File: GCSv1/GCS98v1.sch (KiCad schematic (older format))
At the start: 23 parts, among them U1 STM32F303CCTx

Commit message: fixed switches in matrix, ready for layout
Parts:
- removed U?: LD3985M33R_SOT23, Package_TO_SOT_SMD:SOT-23-5, symbol Regulator_Linear:LD3985M33R_SOT23
- added U2: LD3985M33R_SOT23, Package_TO_SOT_SMD:SOT-23-5, symbol Regulator_Linear:LD3985M33R_SOT23
- C10, C11, C12, C13, C14, C15, C16, C17, C7, C8, C9: renamed from C?; footprint (none) -> Capacitor_SMD:C_0805_2012Metric_Pad1.18x1.45mm_HandSolder
- C18: renamed from 100nF; value C -> 100nF; footprint (none) -> Capacitor_SMD:C_0805_2012Metric_Pad1.18x1.45mm_HandSolder
- R2, R3, R4, R5: renamed from R?; footprint (none) -> Resistor_SMD:R_0805_2012Metric_Pad1.20x1.40mm_HandSolder
- SW99: renamed from SW?; footprint (none) -> Button_Switch_SMD:SW_SPST_SKQG_WithStem
- Y1: renamed from Y?; footprint (none) -> Crystal:Crystal_SMD_3225-4Pin_3.2x2.5mm_HandSoldering
- gave numbers to parts that had none: 3
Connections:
- net +5V: now also U2.1 (VIN), U2.3 (INH)
- net GND: now also U2.2 (GND)
- net at C10.1: now also U2.4 (BYP)
- net at C11.1, C8.1, D197.2 (A): now also U2.5 (VOUT)
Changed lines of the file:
@@
 $EndSheet
 $Comp
-L Connector_Generic:Conn_01x04 J?
+L Connector_Generic:Conn_01x04 J1
 U 1 1 6100B131
 P 5900 4550
-F 0 "J?" H 5980 4542 50  0000 L CNN
+F 0 "J1" H 5980 4542 50  0000 L CNN
 F 1 "SM04B-SRSS-TB(LF)(SN)" H 5980 4451 50  0000 L CNN
 F 2 "random-keyboard-parts:JST-SR-4" H 5900 4550 50  0001 C CNN
@@
 	3750 2150 3650 2150
 $Comp
-L Regulator_Linear:LD3985M33R_SOT23 U?
-U 1 1 61021750
-P 3800 1100
-F 0 "U?" H 3800 1442 50  0000 C CNN
-F 1 "LD3985M33R_SOT23" H 3800 1351 50  0000 C CNN
-F 2 "Package_TO_SOT_SMD:SOT-23-5" H 3800 1425 50  0001 C CIN
-F 3 "http://www.st.com/internet/com/TECHNICAL_RESOURCES/TECHNICAL_LITERATURE/DATASHEET/CD00003395.pdf" H 3800 1100 50  0001 C CNN
-	1    3800 1100
-	1    0    0    -1
-$EndComp
-$Comp
 L power:+3V3 #PWR0103
 U 1 1 6102369C
@@
 $EndComp
 $Comp
-L Device:C C?
+L Device:C C7
 U 1 1 610250E6
 P 3100 1250
-F 0 "C?" H 3215 1296 50  0000 L CNN
+F 0 "C7" H 3215 1296 50  0000 L CNN
 F 1 "1µF" H 3215 1205 50  0000 L CNN
-F 2 "" H 3138 1100 50  0001 C CNN
+F 2 "Capacitor_SMD:C_0805_2012Metric_Pad1.18x1.45mm_HandSolder" H 3138 1100 50  0001 C CNN
 F 3 "~" H 3100 1250 50  0001 C CNN
 	1    3100 1250
@@
 	3100 1000 3100 1100
 $Comp
-L Device:C C?
+L Device:C C9
 U 1 1 6102C881
 P 3400 1400
-F 0 "C?" H 3515 1446 50  0000 L CNN
+F 0 "C9" H 3515 1446 50  0000 L CNN
 F 1 "100nF" H 3515 1355 50  0000 L CNN
-F 2 "" H 3438 1250 50  0001 C CNN
+F 2 "Capacitor_SMD:C_0805_2012Metric_Pad1.18x1.45mm_HandSolder" H 3438 1250 50  0001 C CNN
 F 3 "~" H 3400 1400 50  0001 C CNN
 	1    3400 1400
@@
 $EndComp
 $Comp
-L Device:C C?
+L Device:C C10
 U 1 1 6102FE4B
 P 4150 1400
-F 0 "C?" H 4265 1446 50  0000 L CNN
+F 0 "C10" H 4265 1446 50  0000 L CNN
 F 1 "10nF" H 4265 1355 50  0000 L CNN
-F 2 "" H 4188 1250 50  0001 C CNN
+F 2 "Capacitor_SMD:C_0805_2012Metric_Pad1.18x1.45mm_HandSolder" H 4188 1250 50  0001 C CNN
 F 3 "~" H 4150 1400 50  0001 C CNN
 	1    4150 1400
@@
 $EndComp
 $Comp
-L Device:C C?
+L Device:C C8
 U 1 1 61037105
 P 4500 1250
-F 0 "C?" H 4615 1296 50  0000 L CNN
+F 0 "C8" H 4615 1296 50  0000 L CNN
 F 1 "100nF" H 4615 1205 50  0000 L CNN
-F 2 "" H 4538 1100 50  0001 C CNN
+F 2 "Capacitor_SMD:C_0805_2012Metric_Pad1.18x1.45mm_HandSolder" H 4538 1100 50  0001 C CNN
 F 3 "~" H 4500 1250 50  0001 C CNN
 	1    4500 1250
@@
 	4500 1100 4500 1000
 $Comp
-L Device:C C?
+L Device:C C11
 U 1 1 61039CE0
 P 4900 1400
-F 0 "C?" H 5015 1446 50  0000 L CNN
+F 0 "C11" H 5015 1446 50  0000 L CNN
 F 1 "100nF" H 5015 1355 50  0000 L CNN
-F 2 "" H 4938 1250 50  0001 C CNN
+F 2 "Capacitor_SMD:C_0805_2012Metric_Pad1.18x1.45mm_HandSolder" H 4938 1250 50  0001 C CNN
 F 3 "~" H 4900 1400 50  0001 C CNN
 	1    4900 1400
@@
 $EndComp
 $Comp
-L Diode:BAT60A D?
+L Diode:BAT60A D197
 U 1 1 6103C710
 P 5150 1000
-F 0 "D?" H 5150 783 50  0000 C CNN
+F 0 "D197" H 5150 783 50  0000 C CNN
 F 1 "BAT60A" H 5150 874 50  0000 C CNN
 F 2 "Diode_SMD:D_SOD-323" H 5150 825 50  0001 C CNN
@@
 $EndComp
 $Comp
-L Device:C C?
+L Device:C C12
 U 1 1 6109CA20
 P 5000 2900
-F 0 "C?" H 5115 2946 50  0000 L CNN
+F 0 "C12" H 5115 2946 50  0000 L CNN
 F 1 "100nF" H 5115 2855 50  0000 L CNN
-F 2 "" H 5038 2750 50  0001 C CNN
+F 2 "Capacitor_SMD:C_0805_2012Metric_Pad1.18x1.45mm_HandSolder" H 5038 2750 50  0001 C CNN
 F 3 "~" H 5000 2900 50  0001 C CNN
 	1    5000 2900
@@
 $EndComp
 $Comp
-L Device:C C?
+L Device:C C13
 U 1 1 6109D7C4
 P 5450 2900
-F 0 "C?" H 5565 2946 50  0000 L CNN
+F 0 "C13" H 5565 2946 50  0000 L CNN
 F 1 "100nF" H 5565 2855 50  0000 L CNN
-F 2 "" H 5488 2750 50  0001 C CNN
+F 2 "Capacitor_SMD:C_0805_2012Metric_Pad1.18x1.45mm_HandSolder" H 5488 2750 50  0001 C CNN
 F 3 "~" H 5450 2900 50  0001 C CNN
 	1    5450 2900
@@
 $EndComp
 $Comp
-L Device:C C?
+L Device:C C14
 U 1 1 610A0182
 P 5900 2900
-F 0 "C?" H 6015 2946 50  0000 L CNN
+F 0 "C14" H 6015 2946 50  0000 L CNN
 F 1 "100nF" H 6015 2855 50  0000 L CNN
-F 2 "" H 5938 2750 50  0001 C CNN
+F 2 "Capacitor_SMD:C_0805_2012Metric_Pad1.18x1.45mm_HandSolder" H 5938 2750 50  0001 C CNN
 F 3 "~" H 5900 2900 50  0001 C CNN
 	1    5900 2900
@@
 $EndComp
 $Comp
-L Device:C C?
+L Device:C C15
 U 1 1 610A0188
 P 6350 2900
-F 0 "C?" H 6465 2946 50  0000 L CNN
+F 0 "C15" H 6465 2946 50  0000 L CNN
 F 1 "100nF" H 6465 2855 50  0000 L CNN
-F 2 "" H 6388 2750 50  0001 C CNN
+F 2 "Capacitor_SMD:C_0805_2012Metric_Pad1.18x1.45mm_HandSolder" H 6388 2750 50  0001 C CNN
 F 3 "~" H 6350 2900 50  0001 C CNN
 	1    6350 2900
@@
 Connection ~ 3750 2150
 $Comp
-L Device:C 100nF
+L Device:C C18
 U 1 1 610C060F
 P 1100 2650
-F 0 "100nF" V 848 2650 50  0000 C CNN
-F 1 "C" V 939 2650 50  0000 C CNN
-F 2 "" H 1138 2500 50  0001 C CNN
+F 0 "C18" V 848 2650 50  0000 C CNN
+F 1 "100nF" V 939 2650 50  0000 C CNN
+F 2 "Capacitor_SMD:C_0805_2012Metric_Pad1.18x1.45mm_HandSolder" H 1138 2500 50  0001 C CNN
 F 3 "~" H 1100 2650 50  0001 C CNN
 	1    1100 2650
@@
 $EndComp
 $Comp
-L Switch:SW_Push SW?
+L Switch:SW_Push SW99
 U 1 1 610C66B5
 P 1100 2300
-F 0 "SW?" H 1100 2585 50  0000 C CNN
+F 0 "SW99" H 1100 2585 50  0000 C CNN
 F 1 "SW_Push" H 1100 2494 50  0000 C CNN
-F 2 "" H 1100 2500 50  0001 C CNN
+F 2 "Button_Switch_SMD:SW_SPST_SKQG_WithStem" H 1100 2500 50  0001 C CNN
 F 3 "~" H 1100 2500 50  0001 C CNN
 	1    1100 2300
@@
 Connection ~ 3550 5250
 $Comp
-L Device:R R?
+L Device:R R3
 U 1 1 610E8EAE
 P 800 3200
-F 0 "R?" H 870 3246 50  0000 L CNN
+F 0 "R3" H 870 3246 50  0000 L CNN
 F 1 "100K" H 870 3155 50  0000 L CNN
-F 2 "" V 730 3200 50  0001 C CNN
+F 2 "Resistor_SMD:R_0805_2012Metric_Pad1.20x1.40mm_HandSolder" V 730 3200 50  0001 C CNN
 F 3 "~" H 800 3200 50  0001 C CNN
 	1    800  3200
@@
 	800  3350 800  3450
 $Comp
-L Diode:BAT60A D?
+L Diode:BAT60A D198
 U 1 1 610F621C
 P 5600 4100
-F 0 "D?" H 5600 3883 50  0000 C CNN
+F 0 "D198" H 5600 3883 50  0000 C CNN
 F 1 "BAT60A" H 5600 3974 50  0000 C CNN
 F 2 "Diode_SMD:D_SOD-323" H 5600 3925 50  0001 C CNN
@@
 Connection ~ 3550 2150
 $Comp
-L Device:Crystal_GND24 Y?
+L Device:Crystal_GND24 Y1
 U 1 1 61135795
 P 1500 4050
-F 0 "Y?" H 1694 4096 50  0000 L CNN
+F 0 "Y1" H 1694 4096 50  0000 L CNN
 F 1 "16MHz" H 1694 4005 50  0000 L CNN
-F 2 "" H 1500 4050 50  0001 C CNN
+F 2 "Crystal:Crystal_SMD_3225-4Pin_3.2x2.5mm_HandSoldering" H 1500 4050 50  0001 C CNN
 F 3 "~" H 1500 4050 50  0001 C CNN
 	1    1500 4050
@@
 $EndComp
 $Comp
-L Device:C C?
+L Device:C C16
 U 1 1 611423E1
 P 1100 4350
-F 0 "C?" H 1215 4396 50  0000 L CNN
+F 0 "C16" H 1215 4396 50  0000 L CNN
 F 1 "20pF" H 1215 4305 50  0000 L CNN
-F 2 "" H 1138 4200 50  0001 C CNN
+F 2 "Capacitor_SMD:C_0805_2012Metric_Pad1.18x1.45mm_HandSolder" H 1138 4200 50  0001 C CNN
 F 3 "~" H 1100 4350 50  0001 C CNN
 	1    1100 4350
@@
 $EndComp
 $Comp
-L Device:C C?
+L Device:C C17
 U 1 1 61143C72
 P 2000 4350
-F 0 "C?" H 2115 4396 50  0000 L CNN
+F 0 "C17" H 2115 4396 50  0000 L CNN
 F 1 "20pF" H 2115 4305 50  0000 L CNN
-F 2 "" H 2038 4200 50  0001 C CNN
+F 2 "Capacitor_SMD:C_0805_2012Metric_Pad1.18x1.45mm_HandSolder" H 2038 4200 50  0001 C CNN
 F 3 "~" H 2000 4350 50  0001 C CNN
 	1    2000 4350
@@
 $EndComp
 $Comp
-L Device:R R?
+L Device:R R2
 U 1 1 611663E7
 P 2300 3000
-F 0 "R?" V 2093 3000 50  0000 C CNN
+F 0 "R2" V 2093 3000 50  0000 C CNN
 F 1 "10K" V 2184 3000 50  0000 C CNN
-F 2 "" V 2230 3000 50  0001 C CNN
+F 2 "Resistor_SMD:R_0805_2012Metric_Pad1.20x1.40mm_HandSolder" V 2230 3000 50  0001 C CNN
 F 3 "~" H 2300 3000 50  0001 C CNN
 	1    2300 3000
@@
 $EndComp
 $Comp
-L Device:R R?
+L Device:R R4
 U 1 1 6117749F
 P 2300 3300
-F 0 "R?" V 2093 3300 50  0000 C CNN
+F 0 "R4" V 2093 3300 50  0000 C CNN
 F 1 "10K" V 2184 3300 50  0000 C CNN
-F 2 "" V 2230 3300 50  0001 C CNN
+F 2 "Resistor_SMD:R_0805_2012Metric_Pad1.20x1.40mm_HandSolder" V 2230 3300 50  0001 C CNN
 F 3 "~" H 2300 3300 50  0001 C CNN
 	1    2300 3300
@@
 $EndComp
 $Comp
-L Device:R R?
+L Device:R R5
 U 1 1 61080E46
 P 5200 4450
-F 0 "R?" H 5270 4496 50  0000 L CNN
+F 0 "R5" H 5270 4496 50  0000 L CNN
 F 1 "1K5" H 5270 4405 50  0000 L CNN
-F 2 "" V 5130 4450 50  0001 C CNN
+F 2 "Resistor_SMD:R_0805_2012Metric_Pad1.20x1.40mm_HandSolder" V 5130 4450 50  0001 C CNN
 F 3 "~" H 5200 4450 50  0001 C CNN
 	1    5200 4450
 	1    0    0    -1
 $EndComp
+$Comp
+L Regulator_Linear:LD3985M33R_SOT23 U2
+U 1 1 66DF6094
+P 3800 1100
+F 0 "U2" H 3800 1442 50  0000 C CNN
+F 1 "LD3985M33R_SOT23" H 3800 1351 50  0000 C CNN
+F 2 "Package_TO_SOT_SMD:SOT-23-5" H 3800 1425 50  0001 C CIN
+F 3 "http://www.st.com/internet/com/TECHNICAL_RESOURCES/TECHNICAL_LITERATURE/DATASHEET/CD00003395.pdf" H 3800 1100 50  0001 C CNN
+	1    3800 1100
+	1    0    0    -1
+$EndComp

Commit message: preliminary work on USB hub
The Texas Instruments USB hub that is currently in there seems like the ticket, but I am still not sure about how USB C connectors will work with the hub IC since it is only for USB 2.0. The main issue is that USB 3.0 and up natively support 3 different power delivery modes up to 15W (and USB power delivery supporting up to 100W), but this is higher than USB 2.0 capabilities and I don't want to fry the thing.
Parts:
- removed D198: BAT60A, Diode_SMD:D_SOD-323, symbol Diode:BAT60A
- removed J1: SM04B-SRSS-TB(LF)(SN), random-keyboard-parts:JST-SR-4, symbol Connector_Generic:Conn_01x04
- removed R5: 1K5, Resistor_SMD:R_0805_2012Metric_Pad1.20x1.40mm_HandSolder, symbol Device:R
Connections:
- net DN renamed DN1
- net DP renamed DP1
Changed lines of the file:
@@
 $Descr A4 11693 8268
 encoding utf-8
-Sheet 1 2
+Sheet 1 3
 Title ""
 Date ""
@@
 F1 "matrix.sch" 50
 $EndSheet
-$Comp
-L Connector_Generic:Conn_01x04 J1
-U 1 1 6100B131
-P 5900 4550
-F 0 "J1" H 5980 4542 50  0000 L CNN
-F 1 "SM04B-SRSS-TB(LF)(SN)" H 5980 4451 50  0000 L CNN
-F 2 "random-keyboard-parts:JST-SR-4" H 5900 4550 50  0001 C CNN
-F 3 "~" H 5900 4550 50  0001 C CNN
-	1    5900 4550
-	1    0    0    -1
-$EndComp
-$Comp
-L power:+5V #PWR0101
-U 1 1 6100BF06
-P 5600 3950
-F 0 "#PWR0101" H 5600 3800 50  0001 C CNN
-F 1 "+5V" H 5615 4123 50  0000 C CNN
-F 2 "" H 5600 3950 50  0001 C CNN
-F 3 "" H 5600 3950 50  0001 C CNN
-	1    5600 3950
-	1    0    0    -1
-$EndComp
-$Comp
-L power:GND #PWR0102
-U 1 1 6100D0BD
-P 5600 4850
-F 0 "#PWR0102" H 5600 4600 50  0001 C CNN
-F 1 "GND" H 5605 4677 50  0000 C CNN
-F 2 "" H 5600 4850 50  0001 C CNN
-F 3 "" H 5600 4850 50  0001 C CNN
-	1    5600 4850
-	1    0    0    -1
-$EndComp
-Wire Wire Line
-	5700 4750 5600 4750
-Wire Wire Line
-	5600 4750 5600 4850
-Wire Wire Line
-	5700 4450 5600 4450
-Wire Wire Line
-	5700 4550 5600 4550
-Text GLabel 5600 4550 0    50   Input ~ 0
-DN
 Text GLabel 4250 4700 2    50   Input ~ 0
-DP
+DP1
 Text GLabel 4250 4600 2    50   Input ~ 0
-DN
+DN1
 $Comp
 L MCU_ST_STM32F3:STM32F303CCTx U1
@@
 Wire Wire Line
 	800  3350 800  3450
-$Comp
-L Diode:BAT60A D198
-U 1 1 610F621C
-P 5600 4100
-F 0 "D198" H 5600 3883 50  0000 C CNN
-F 1 "BAT60A" H 5600 3974 50  0000 C CNN
-F 2 "Diode_SMD:D_SOD-323" H 5600 3925 50  0001 C CNN
-F 3 "https://www.digikey.com/en/products/detail/stmicroelectronics/BAT60JFILM/686386" H 5600 4100 50  0001 C CNN
-	1    5600 4100
-	0    1    1    0
-$EndComp
-Wire Wire Line
-	5600 4250 5600 4450
 Text GLabel 1400 2650 2    50   Input ~ 0
 NRST
@@
 Wire Wire Line
 	2600 3200 2950 3200
-Text GLabel 5100 4650 0    50   Input ~ 0
-DP
-Wire Wire Line
-	5200 4650 5100 4650
-Wire Wire Line
-	5200 4650 5700 4650
-Connection ~ 5200 4650
-Wire Wire Line
-	5200 4600 5200 4650
-Wire Wire Line
-	5200 4300 5200 4200
-$Comp
-L power:+3V3 #PWR0116
-U 1 1 61081D73
-P 5200 4200
-F 0 "#PWR0116" H 5200 4050 50  0001 C CNN
-F 1 "+3V3" H 5215 4373 50  0000 C CNN
-F 2 "" H 5200 4200 50  0001 C CNN
-F 3 "" H 5200 4200 50  0001 C CNN
-	1    5200 4200
-	1    0    0    -1
-$EndComp
-$Comp
-L Device:R R5
-U 1 1 61080E46
-P 5200 4450
-F 0 "R5" H 5270 4496 50  0000 L CNN
-F 1 "1K5" H 5270 4405 50  0000 L CNN
-F 2 "Resistor_SMD:R_0805_2012Metric_Pad1.20x1.40mm_HandSolder" V 5130 4450 50  0001 C CNN
-F 3 "~" H 5200 4450 50  0001 C CNN
-	1    5200 4450
-	1    0    0    -1
-$EndComp
 $Comp
 L Regulator_Linear:LD3985M33R_SOT23 U2
@@
 	1    0    0    -1
 $EndComp
+$Sheet
+S 7550 900  3050 850
+U 611E8410
+F0 "USB_hub" 50
+F1 "USB_hub.sch" 50
+$EndSheet
 $EndSCHEMATC

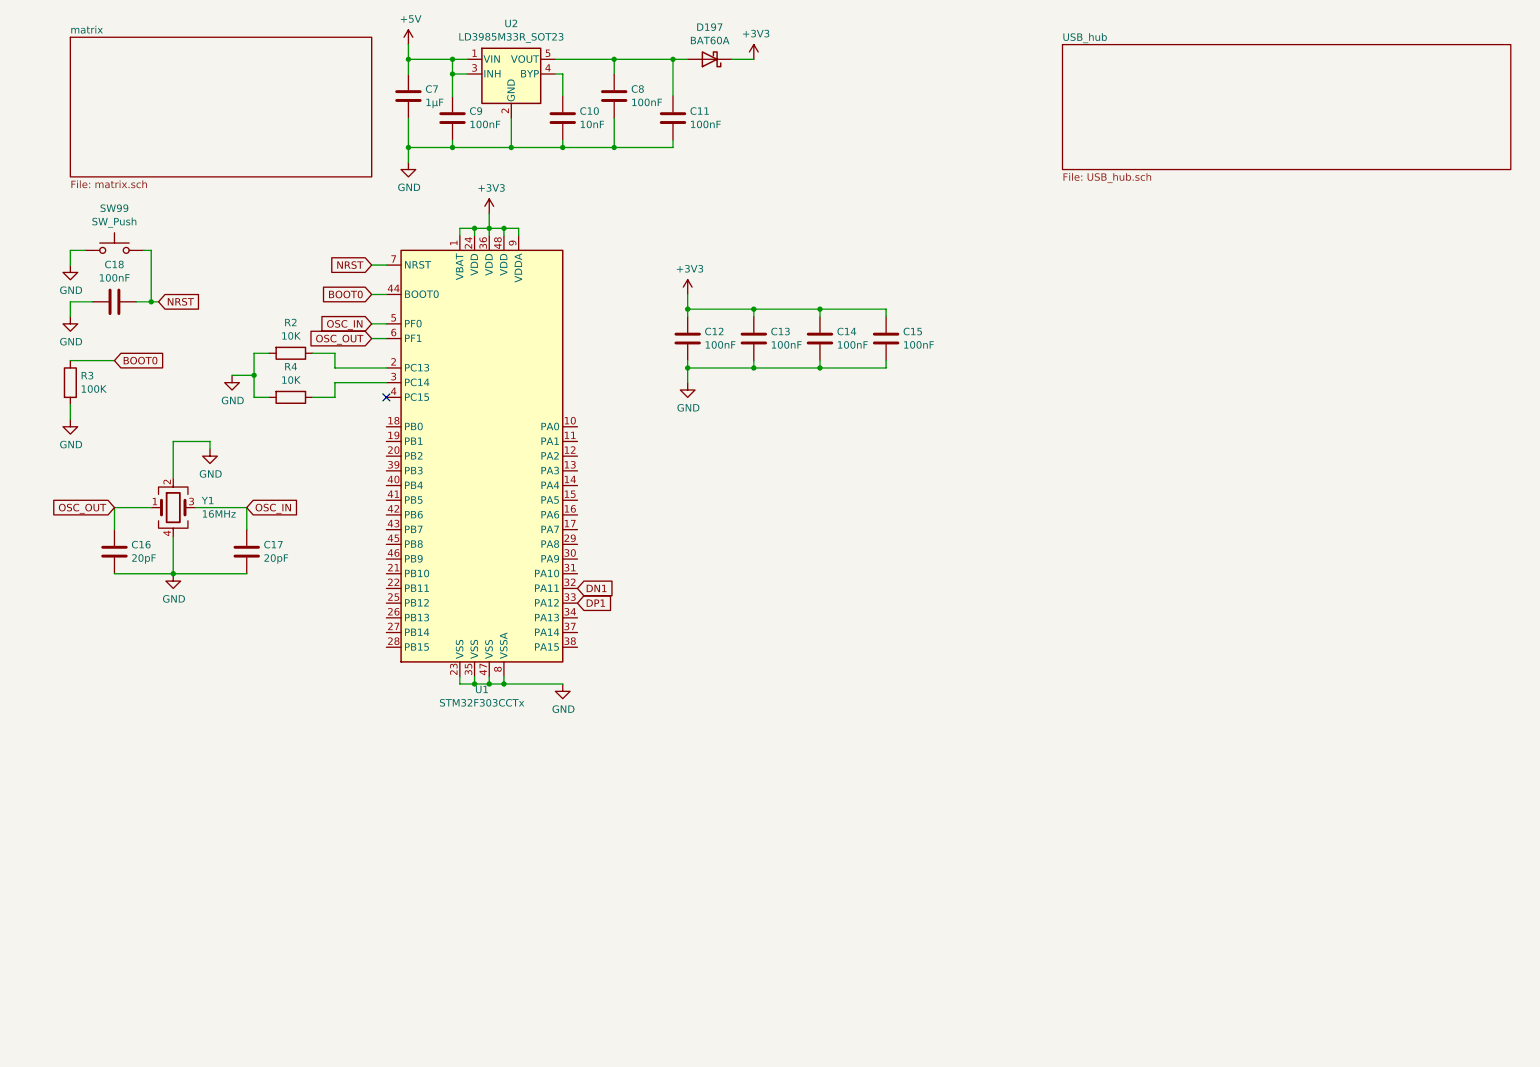
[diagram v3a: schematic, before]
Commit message: redid matrix routing, not doing USB daughter board because of parts availability
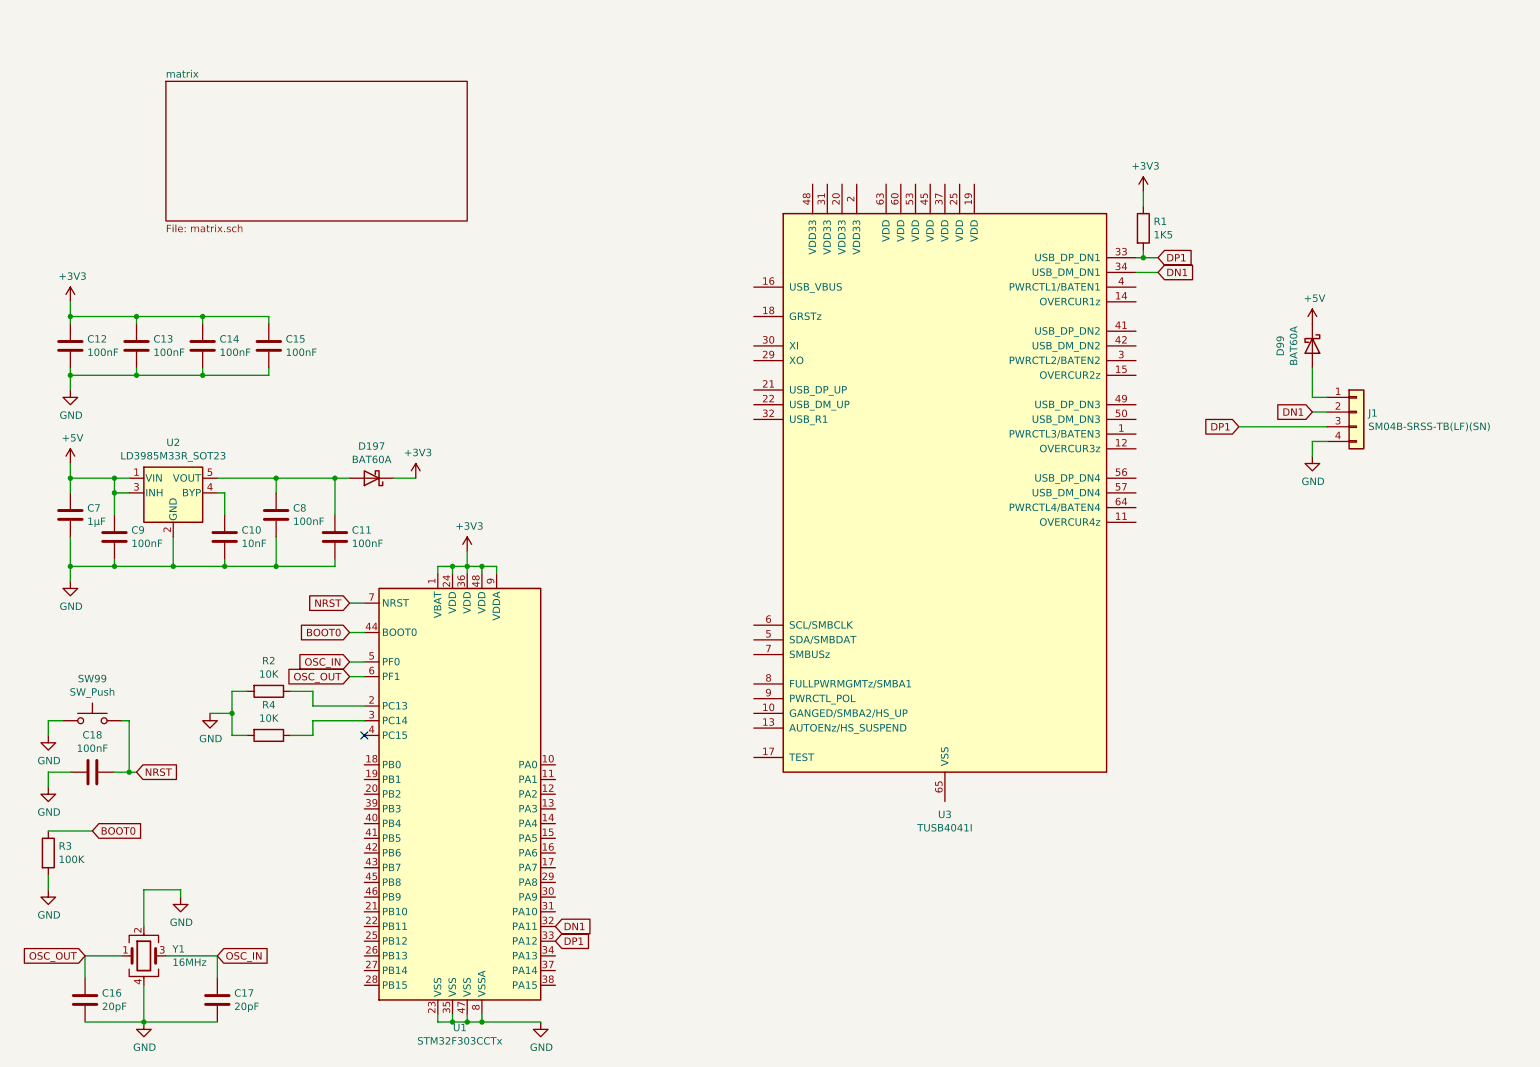
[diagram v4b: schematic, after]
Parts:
- added D99: BAT60A, Diode_SMD:D_SOD-323, symbol Diode:BAT60A
- added J1: SM04B-SRSS-TB(LF)(SN), random-keyboard-parts:JST-SR-4, symbol Connector_Generic:Conn_01x04
- added R1: 1K5, Resistor_SMD:R_0805_2012Metric_Pad1.20x1.40mm_HandSolder, symbol Device:R
- added U3: TUSB4041I, Package_QFP:HTQFP-64-1EP_10x10mm_P0.5mm_EP8x8mm_Mask4.4x4.4mm_ThermalVias, symbol Interface_USB:TUSB4041I
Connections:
- net +3V3: now also R1.1
- net +5V: now also D99.1 (K)
- net DN1: now also J1.2 (Pin_2), U3.34 (USB_DM_DN1)
- net DP1: now also J1.3 (Pin_3), R1.2, U3.33 (USB_DP_DN1)
- net GND: now also J1.4 (Pin_4)
- new net: D99.2 (A), J1.1 (Pin_1)
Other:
- moved on the sheet: C10, C11, C12, C13, C14, C15, C16, C17, C18, C7, C8, C9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
